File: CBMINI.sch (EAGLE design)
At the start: 47 parts, among them J1 USB_B_PTH, SW1 SWITCH-DPDT3, U1 MCP2551, X1 INPUT, X2 OUTPUT

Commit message: Changed CAN crystal to 16MHz for compatibility with Arduino CAN shields
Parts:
- XTL2: value 8MHz -> 16MHz
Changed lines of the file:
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@@
 <part name="U$10" library="SparkFun" deviceset="5V" device=""/>
 <part name="C7" library="freetronics-master-v1.1" deviceset="CAP" device="0603" value="15pF"/>
-<part name="XTL2" library="freetronics-jon" deviceset="CRYSTAL-GND" device="3X2" value="8MHz"/>
+<part name="XTL2" library="freetronics-jon" deviceset="CRYSTAL-GND" device="3X2" value="16MHz"/>
 <part name="C8" library="freetronics-master-v1.1" deviceset="CAP" device="0603" value="15pF"/>
 <part name="JP1" library="freetronics-jon" deviceset="M04" device="PTH" value="CAN"/>

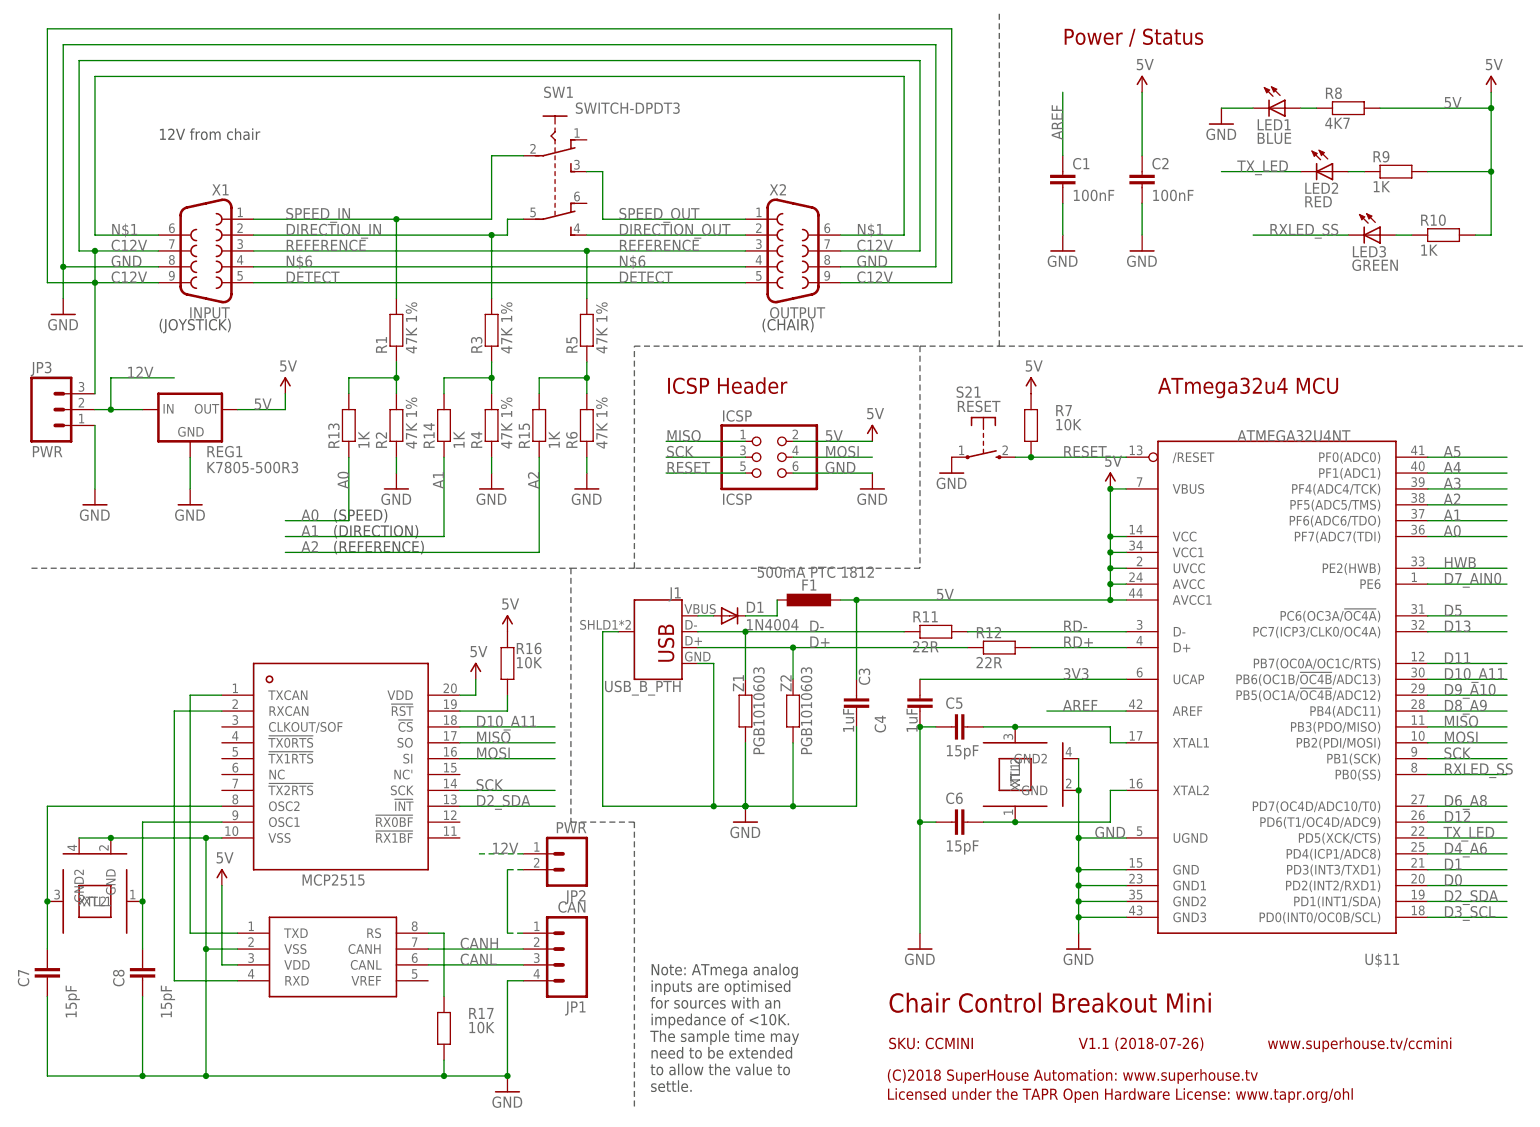
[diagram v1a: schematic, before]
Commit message: Added extra input channels and CAN termination for v2.0 release
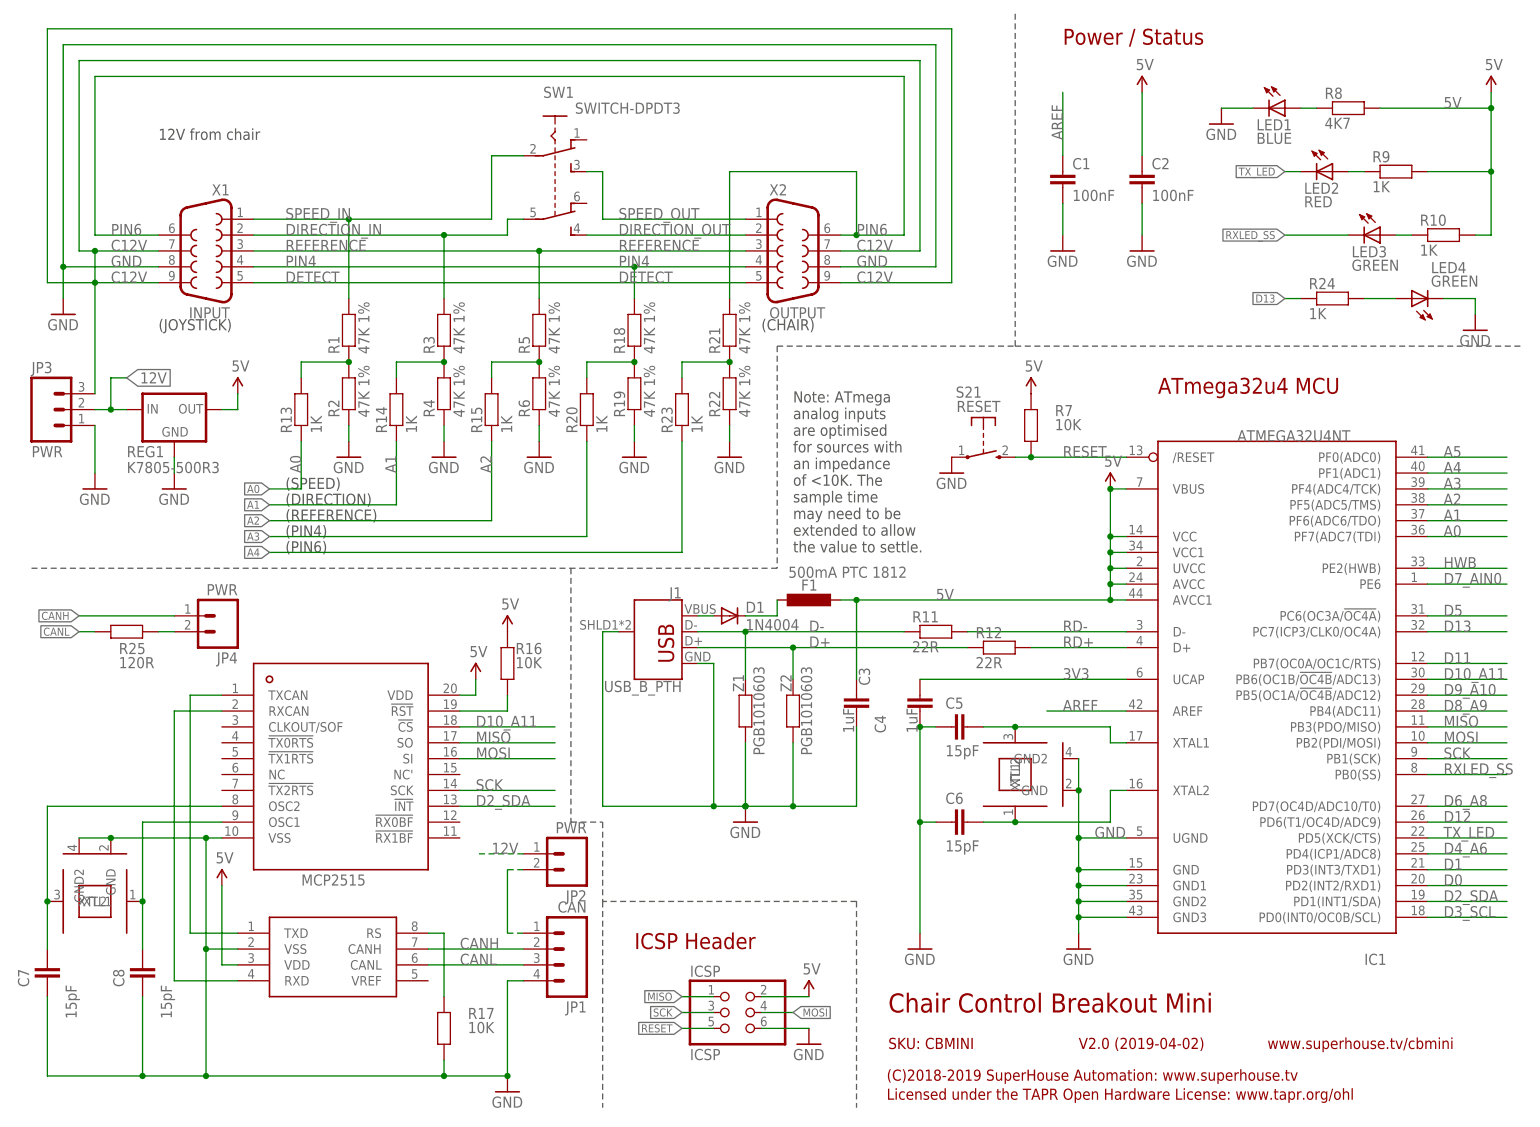
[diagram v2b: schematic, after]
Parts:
- added JP4: PWR, freetronics-jon:M02PTH
- added LED4: GREEN, freetronics-jon:LED0603
- added R18, R19, R21, R22: 47K 1%, freetronics-jon:RESISTOR0603
- added R20, R23, R24: 1K, freetronics-jon:RESISTOR0603
- added R25: 120R, freetronics-master-v1.1:RESISTOR0603
- renumbered U$11 to IC1, U$4 to IC2, U1 to IC3
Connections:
- removed net N$6: X1.4, X2.4
- new net N$19: R18.1, R19.2, R20.2
- new net N$20: JP4.2, R25.2
- new net N$21: R21.1, R22.2, R23.2
- new net PIN4: R18.2, X1.4, X2.4
- new net PIN6: R21.2, X1.6, X2.6
- net A3: now also R20.1
- net A4: now also R23.1
- net CANH: now also JP4.1
- net CANL: now also R25.1
- net D13: now also R24.1
- net GND: now also LED4.C, R19.1, R22.1
- net N$1: now also LED4.A, R24.2; no longer X1.6, X2.6
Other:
- note added: "(C)2018-2019 SuperHouse Automation: www.superhouse.tv"
- note added: "(PIN4)"
- note added: "(PIN6)"
- note added: "SKU: CBMINI"
- note added: "V2.0 (2019-04-02)"
- note added: "www.superhouse.tv/cbmini"
- note removed: "(C)2018 SuperHouse Automation: www.superhouse.tv"
- note removed: "SKU: CCMINI"
- note removed: "V1.1 (2018-07-26)"
- note removed: "www.superhouse.tv/ccmini"
- moved on the sheet: ICSP, R1, R13, R14, R15, R2, R3, R4, R5, R6, REG1
